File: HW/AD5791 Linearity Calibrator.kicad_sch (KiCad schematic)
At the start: 62 parts, among them J10 Conn_01x01, J11 ISO OUT, J12 ISO OUT, J2 PWR, J3 REF, J4 REF, J5 REF, J6 REF, J7 Conn_01x01, J8 Conn_01x01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

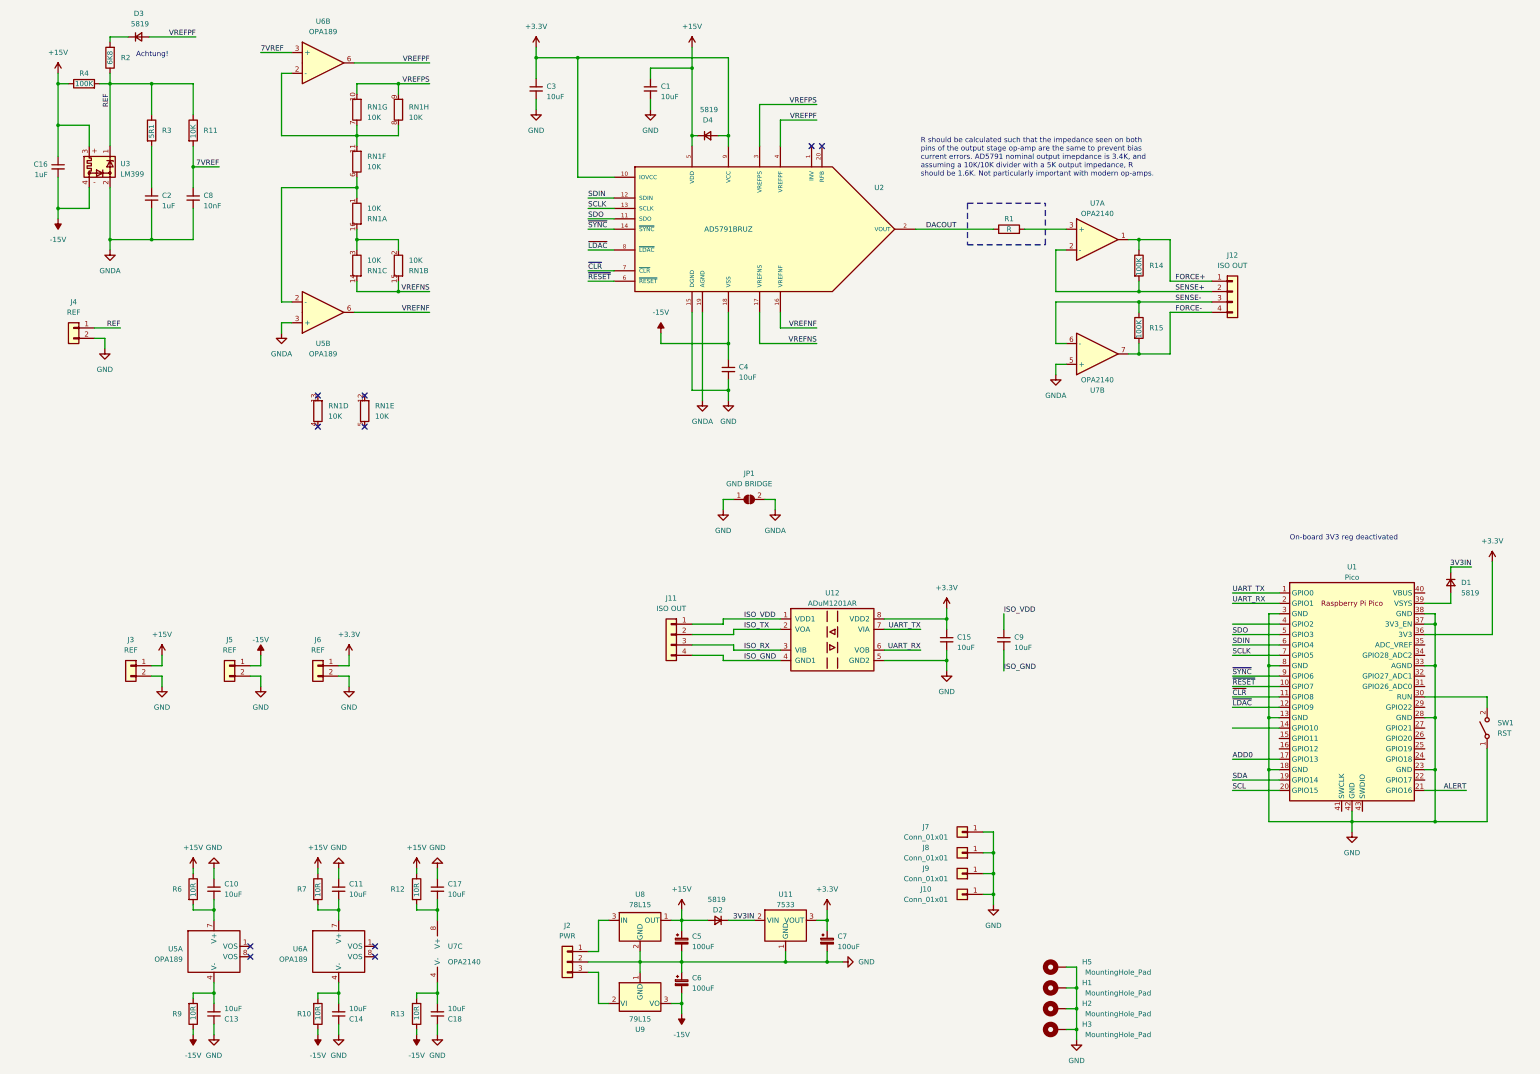
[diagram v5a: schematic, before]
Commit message: post-assembly touch ups
- ground coupling jumper now shorted by default
- software files updated with pinout
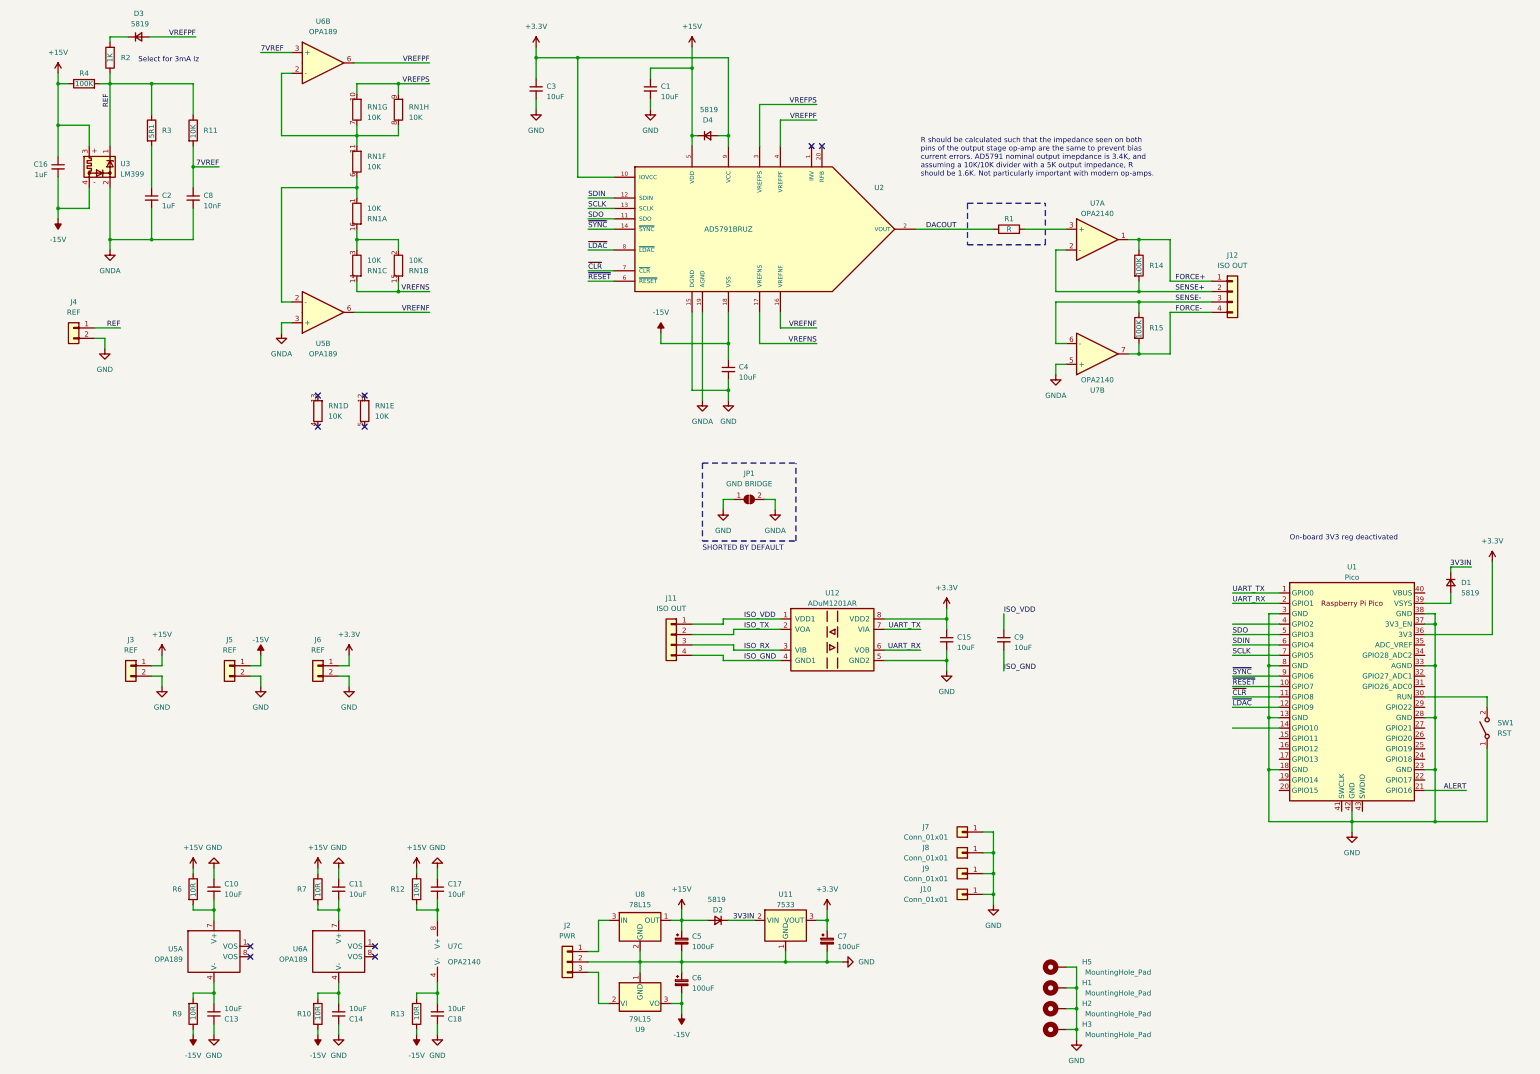
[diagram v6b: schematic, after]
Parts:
- R2: value 6K8 -> 1K
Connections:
- net ADD0: no longer names the net of U1.17 (GPIO13)
- net SCL: no longer names the net of U1.20 (GPIO15)
- net SDA: no longer names the net of U1.19 (GPIO14)
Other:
- note added: "SHORTED BY DEFAULT"
- note added: "Select for 3mA Iz"
- note removed: "Achtung!"
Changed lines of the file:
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@@
     (stroke (width 0) (type default))
+  )
+  (polyline (pts (xy 186.69 133.35) (xy 186.69 152.4))
+    (stroke (width 0) (type dash))
   )
   (wire (pts (xy 161.29 252.73) (xy 161.29 245.11))
@@
     (stroke (width 0) (type default))
   )
-  (wire (pts (xy 316.23 213.36) (xy 327.66 213.36))
-    (stroke (width 0) (type default))
-  )
   (wire (pts (xy 184.15 180.34) (xy 191.77 180.34))
     (stroke (width 0) (type default))
@@
     (stroke (width 0) (type default))
   )
-  (wire (pts (xy 316.23 210.82) (xy 327.66 210.82))
-    (stroke (width 0) (type default))
-  )
   (wire (pts (xy 112.395 88.9) (xy 112.395 91.44))
     (stroke (width 0) (type default))
@@
     (stroke (width 0) (type default))
   )
-  (wire (pts (xy 316.23 205.74) (xy 327.66 205.74))
-    (stroke (width 0) (type default))
-  )
   (wire (pts (xy 116.84 262.89) (xy 121.92 262.89))
     (stroke (width 0) (type default))
@@
     (stroke (width 0) (type default))
   )
+  (polyline (pts (xy 209.55 152.4) (xy 209.55 133.35))
+    (stroke (width 0) (type dash))
+  )
   (wire (pts (xy 378.46 193.04) (xy 378.46 190.5))
     (stroke (width 0) (type default))
@@
     (stroke (width 0) (type default))
   )
+  (polyline (pts (xy 186.69 133.35) (xy 209.55 133.35))
+    (stroke (width 0) (type dash))
+  )
   (wire (pts (xy 179.07 265.43) (xy 181.61 265.43))
     (stroke (width 0) (type default))
@@
     (stroke (width 0) (type default))
   )
+  (polyline (pts (xy 186.69 152.4) (xy 209.55 152.4))
+    (stroke (width 0) (type dash))
+  )
   (wire (pts (xy 121.92 232.41) (xy 121.92 234.95))
     (stroke (width 0) (type default))
@@
   (wire (pts (xy 97.79 232.41) (xy 97.79 234.95))
     (stroke (width 0) (type default))
+  )
+  (text "SHORTED BY DEFAULT" (at 186.69 154.94 0)
+    (effects (font (size 1.27 1.27)) (justify left bottom))
   )
   (text "On-board 3V3 reg deactivated" (at 330.2 152.4 0)
@@
     (effects (font (size 1.27 1.27)) (justify left bottom))
   )
-  (text "Achtung!" (at 48.26 34.29 0)
+  (text " Select for 3mA Iz" (at 48.26 35.56 0)
     (effects (font (size 1.27 1.27)) (justify left bottom))
   )
@@
     (effects (font (size 1.27 1.27)) (justify left bottom))
   )
-  (label "SDA" (at 316.23 210.82 0) (fields_autoplaced)
-    (effects (font (size 1.27 1.27)) (justify left bottom))
-  )
   (label "ISO_GND" (at 196.85 181.61 0) (fields_autoplaced)
     (effects (font (size 1.27 1.27)) (justify left bottom))
@@
     (effects (font (size 1.27 1.27)) (justify right bottom))
   )
-  (label "SCL" (at 316.23 213.36 0) (fields_autoplaced)
-    (effects (font (size 1.27 1.27)) (justify left bottom))
-  )
   (label "VREFPS" (at 120.015 40.64 180) (fields_autoplaced)
     (effects (font (size 1.27 1.27)) (justify right bottom))
-  )
-  (label "ADD0" (at 316.23 205.74 0) (fields_autoplaced)
-    (effects (font (size 1.27 1.27)) (justify left bottom))
   )
   (label "~{CLR}" (at 316.23 190.5 0) (fields_autoplaced)
@@
       (effects (font (size 1.27 1.27)))
     )
-    (property "Value" "6K8" (at 41.91 34.29 90)
-      (effects (font (size 1.27 1.27)))
-    )
+    (property "Value" "1K" (at 41.91 34.29 90)
+      (effects (font (size 1.27 1.27)))
+    )

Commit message: added V2 files
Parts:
- U5, U6: value OPA189 -> ADA4522-1
- U7: value OPA2140 -> ADA4522-2
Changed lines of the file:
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@@
       (effects (font (size 1.27 1.27)) (justify left))
     )
-    (property "Value" "OPA2140" (at 124.46 255.27 0)
+    (property "Value" "ADA4522-2" (at 124.46 255.27 0)
       (effects (font (size 1.27 1.27)) (justify left))
     )
@@
       (effects (font (size 1.27 1.27)))
     )
-    (property "Value" "OPA189" (at 93.98 27.94 0)
+    (property "Value" "ADA4522-1" (at 93.98 27.94 0)
       (effects (font (size 1.27 1.27)))
     )
@@
       (effects (font (size 1.27 1.27)))
     )
-    (property "Value" "OPA2140" (at 283.21 113.03 0)
+    (property "Value" "ADA4522-2" (at 283.21 113.03 0)
       (effects (font (size 1.27 1.27)))
     )
@@
       (effects (font (size 1.27 1.27)))
     )
-    (property "Value" "OPA189" (at 93.98 106.68 0)
+    (property "Value" "ADA4522-1" (at 93.98 106.68 0)
       (effects (font (size 1.27 1.27)))
     )
@@
       (effects (font (size 1.27 1.27)) (justify right))
     )
-    (property "Value" "OPA189" (at 90.17 254.635 0)
+    (property "Value" "ADA4522-1" (at 90.17 254.635 0)
       (effects (font (size 1.27 1.27)) (justify right))
     )
@@
   (symbol (lib_id "Device:Opamp_Dual") (at 283.21 78.74 0) (unit 1)
     (in_bom yes) (on_board yes) (dnp no) (fields_autoplaced)
-    (property "Reference" "U7" (at 283.21 69.85 0)
-      (effects (font (size 1.27 1.27)))
-    )
-    (property "Value" "OPA2140" (at 283.21 72.39 0)
+    (property "Reference" "U7" (at 283.21 68.58 0)
+      (effects (font (size 1.27 1.27)))
+    )
+    (property "Value" "ADA4522-2" (at 283.21 71.12 0)
       (effects (font (size 1.27 1.27)))
     )
@@
       (effects (font (size 1.27 1.27)) (justify right))
     )
-    (property "Value" "OPA189" (at 59.69 254.635 0)
+    (property "Value" "ADA4522-1" (at 59.69 254.635 0)
       (effects (font (size 1.27 1.27)) (justify right))
     )
